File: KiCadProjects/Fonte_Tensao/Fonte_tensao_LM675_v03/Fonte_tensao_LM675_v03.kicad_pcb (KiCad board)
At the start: 2 copper layers, 90 x 100 mm, 30 parts, among them J1 Barrel_Jack, J2 sinais analogicos, J3 comunicacao / sinais digitais, J4 tensoes, U1 L7809, U2 LM7909_TO220, U3 LM675, U4 L7805, U5 L7905, U6 LM1117T-3.3

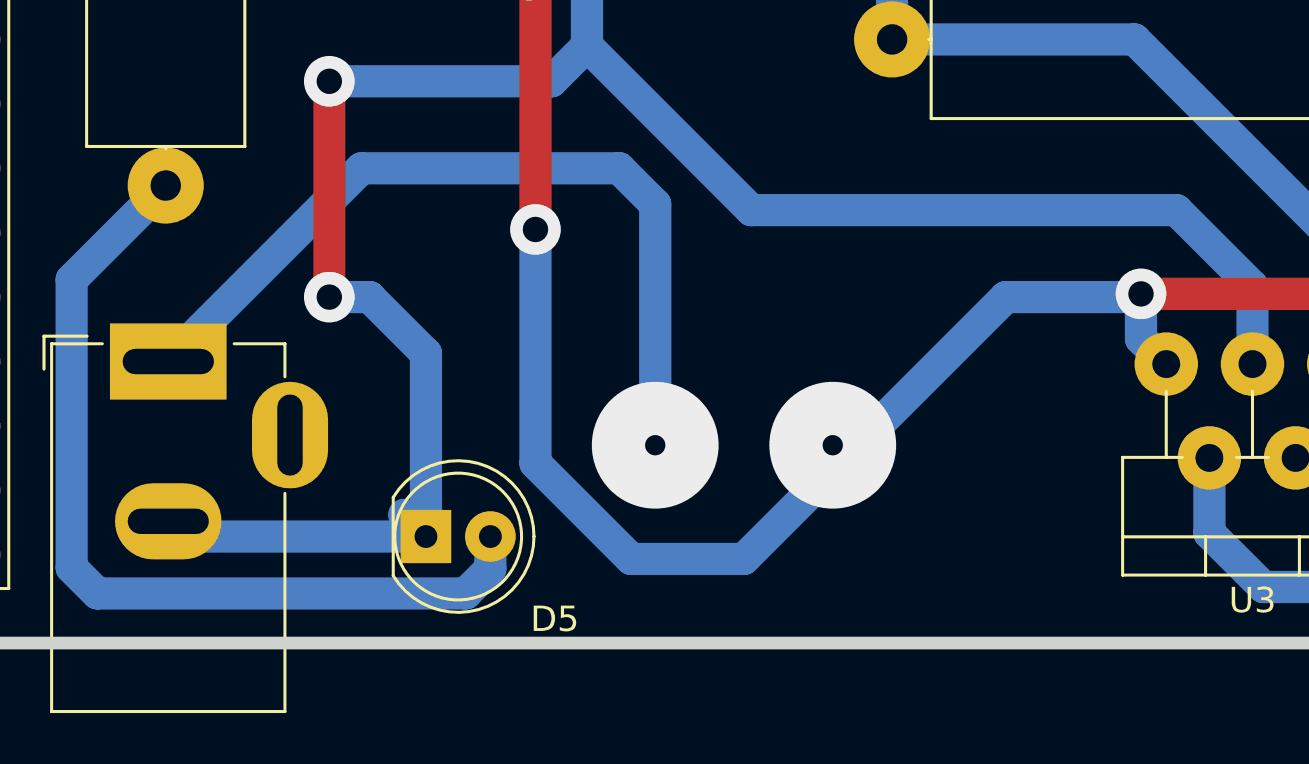
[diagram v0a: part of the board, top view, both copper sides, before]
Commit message: PCB: atualizacao simbolos chave
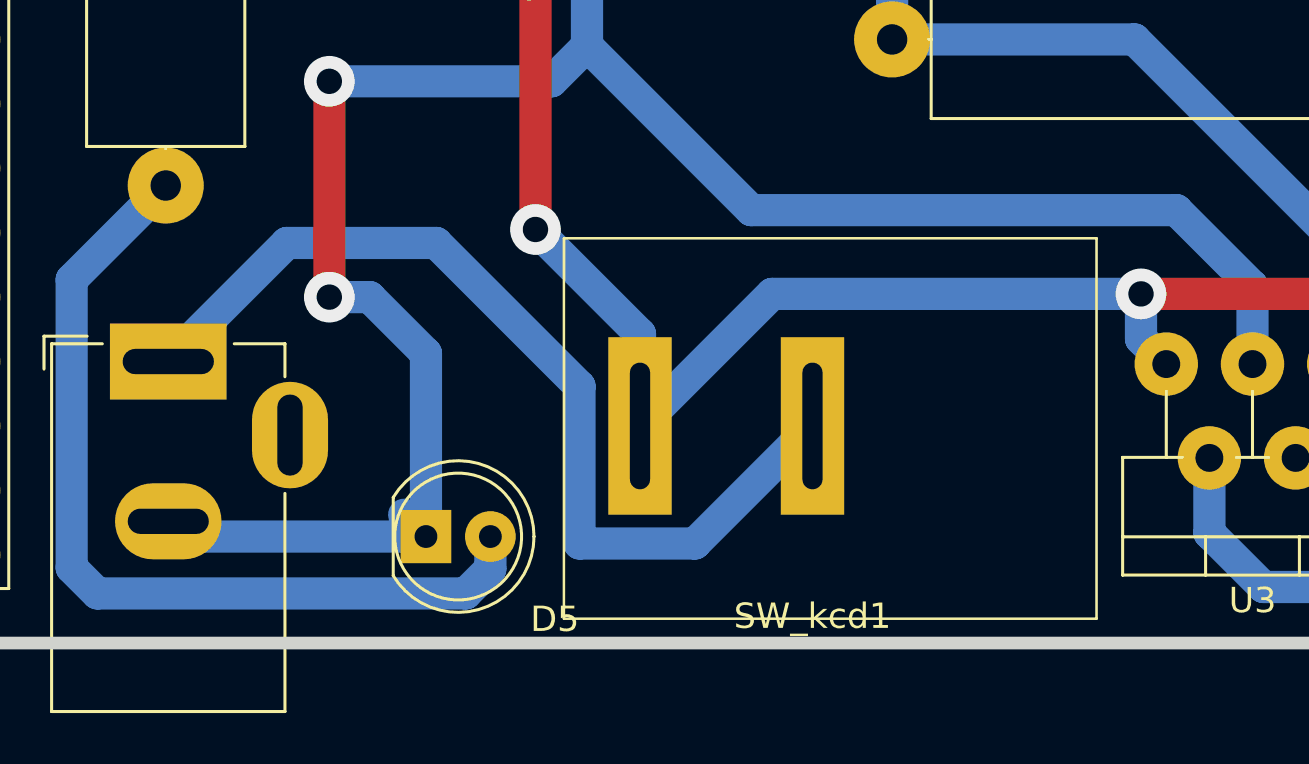
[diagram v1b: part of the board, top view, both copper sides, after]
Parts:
- added SW_kcd1: chave_gangorra_2_pinos, Chave_Gangorra:chave gangorra 2 pinos, F.Cu at (139.7, 150.2)
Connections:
- C1 pad 1: switch -> VCC
- C10 pad 1: switch -> VCC
- J1 pad 1: switch -> Net-(J1-Pad1)
- J4 pad 2: switch -> VCC
- R1 pad 1: switch -> VCC
- R2 pad 1: switch -> VCC
- U1 pad 1: switch -> VCC
- U3 pad 5: switch -> VCC
- U4 pad 1: switch -> VCC
- U6 pad 3: switch -> VCC
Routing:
- net switch: track 234.9 -> 0.00 mm, vias 9 -> 0
- net VCC: track 0.00 -> 194.2 mm, vias 0 -> 7
- net Net-(J1-Pad1): track 0.00 -> 37.8 mm

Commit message: correção valores componentes
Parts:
- C1: value 0.33uF -> 3.3uF
- C2: value 2.2uF -> 22uF
- C4, C8: value 0.1uF -> 1uF
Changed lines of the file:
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@@
         (effects (font (size 1 1) (thickness 0.15)))
     )
-    (fp_text value "2.2uF" (at 1.25 3.75) (layer "F.Fab")
+    (fp_text value "22uF" (at 1.25 3.75) (layer "F.Fab")
         (effects (font (size 1 1) (thickness 0.15)))
     )
@@
         (effects (font (size 1 1) (thickness 0.15)))
     )
-    (fp_text value "0.1uF" (at 1.25 3.75) (layer "F.Fab")
+    (fp_text value "1uF" (at 1.25 3.75) (layer "F.Fab")
         (effects (font (size 1 1) (thickness 0.15)))
     )
@@
         (effects (font (size 1 1) (thickness 0.15)))
     )
-    (fp_text value "0.33uF" (at 1.484 5.08) (layer "F.Fab")
+    (fp_text value "3.3uF" (at 1.484 5.08) (layer "F.Fab")
         (effects (font (size 1 1) (thickness 0.15)))
     )
@@
         (effects (font (size 1 1) (thickness 0.15)))
     )
-    (fp_text value "0.1uF" (at 0.508 -5.08) (layer "F.Fab")
+    (fp_text value "1uF" (at 0.508 -5.08) (layer "F.Fab")
         (effects (font (size 1 1) (thickness 0.15)))
     )
